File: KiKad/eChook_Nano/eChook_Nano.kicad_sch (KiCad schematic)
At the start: 86 parts, among them J1 Expansion, Q2 Q_NMOS-D_Generic_GSD, Q3 Q_NMOS-D_Generic_GSD, U1 Arduino_Nano_v3.x, U2 TSR_1-2450, U3 MCP6002-xP

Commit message: Updated to BAT54S diodes. Added protection on all inputs
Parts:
- removed D1, D2, D4, D5, D6: SBD, Diode_SMD:D_SOD-523, symbol Device:D_Schottky
- added D1, D13, D14, D15, D16, D17, D18, D19, D2, D20, D4, D5, D6: BAT54S, Package_TO_SOT_SMD:SOT-23, symbol Diode:BAT54S
- JP1, JP2: now not fitted
- JP3: value SolderJumper_2_Open -> ~; footprint Jumper:SolderJumper-2_P1.3mm_Open_RoundedPad1.0x1.5mm -> Jumper:SolderJumper-2_P1.3mm_Bridged_RoundedPad1.0x1.5mm; symbol Jumper:SolderJumper_2_Open -> Jumper:SolderJumper_2_Bridged; now not fitted; now in the parts list
- R34: value 10k -> 100k; LCSC C17414 -> (none)
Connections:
- net +5V: now also D1.2 (K), D13.2 (K), D14.2 (K), D15.2 (K), D16.2 (K), D17.2 (K), D18.2 (K), D19.2 (K), D2.2 (K), D20.2 (K), D4.2 (K), D5.2 (K), D6.2 (K)
- net Batt1v: now also D5.3 (COM)
- net BattTotalV: now also D4.3 (COM)
- net Brake: now also D16.3 (COM)
- net DriverButton: now also D17.3 (COM)
- net DriverButton2: now also D18.3 (COM)
- net GND: now also D1.1 (A), D13.1 (A), D14.1 (A), D15.1 (A), D16.1 (A), D17.1 (A), D18.1 (A), D19.1 (A), D2.1 (A), D20.1 (A), D4.1 (A), D5.1 (A), D6.1 (A)
- net MotorRPM: now also D19.3 (COM)
- net Temp1: now also D2.3 (COM)
- net Temp2: now also D1.3 (COM)
- net Throttle: now also D6.3 (COM)
- net WheelRPM: now also D20.3 (COM)
- net at Q3.3 (D), R14.2, R25.1: now also D15.3 (COM)
- net CurrRefIn: now reaches R21.1, R22.2, U3.2 (-)
- net CurrRefIn: now also D13.3 (COM)
- net CurrSenseIn: now reaches R20.1, R23.2, U3.3 (+)
- net CurrSenseIn: now also D14.3 (COM)
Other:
- note added: "Bluetooth Header"
- note added: "Button Inputs"
- note added: "Expansion Header"
- note added: "PWM Output"
- note removed: "Bluetooth Module"
- note removed: "Driver Input"
- note removed: "Expansion Port"
- note removed: "PWM Buffer"
- moved on the sheet: C4, C5, Conn1, Conn4, Conn5, Conn6, Conn7, Conn8, D10, D11, D3, D8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

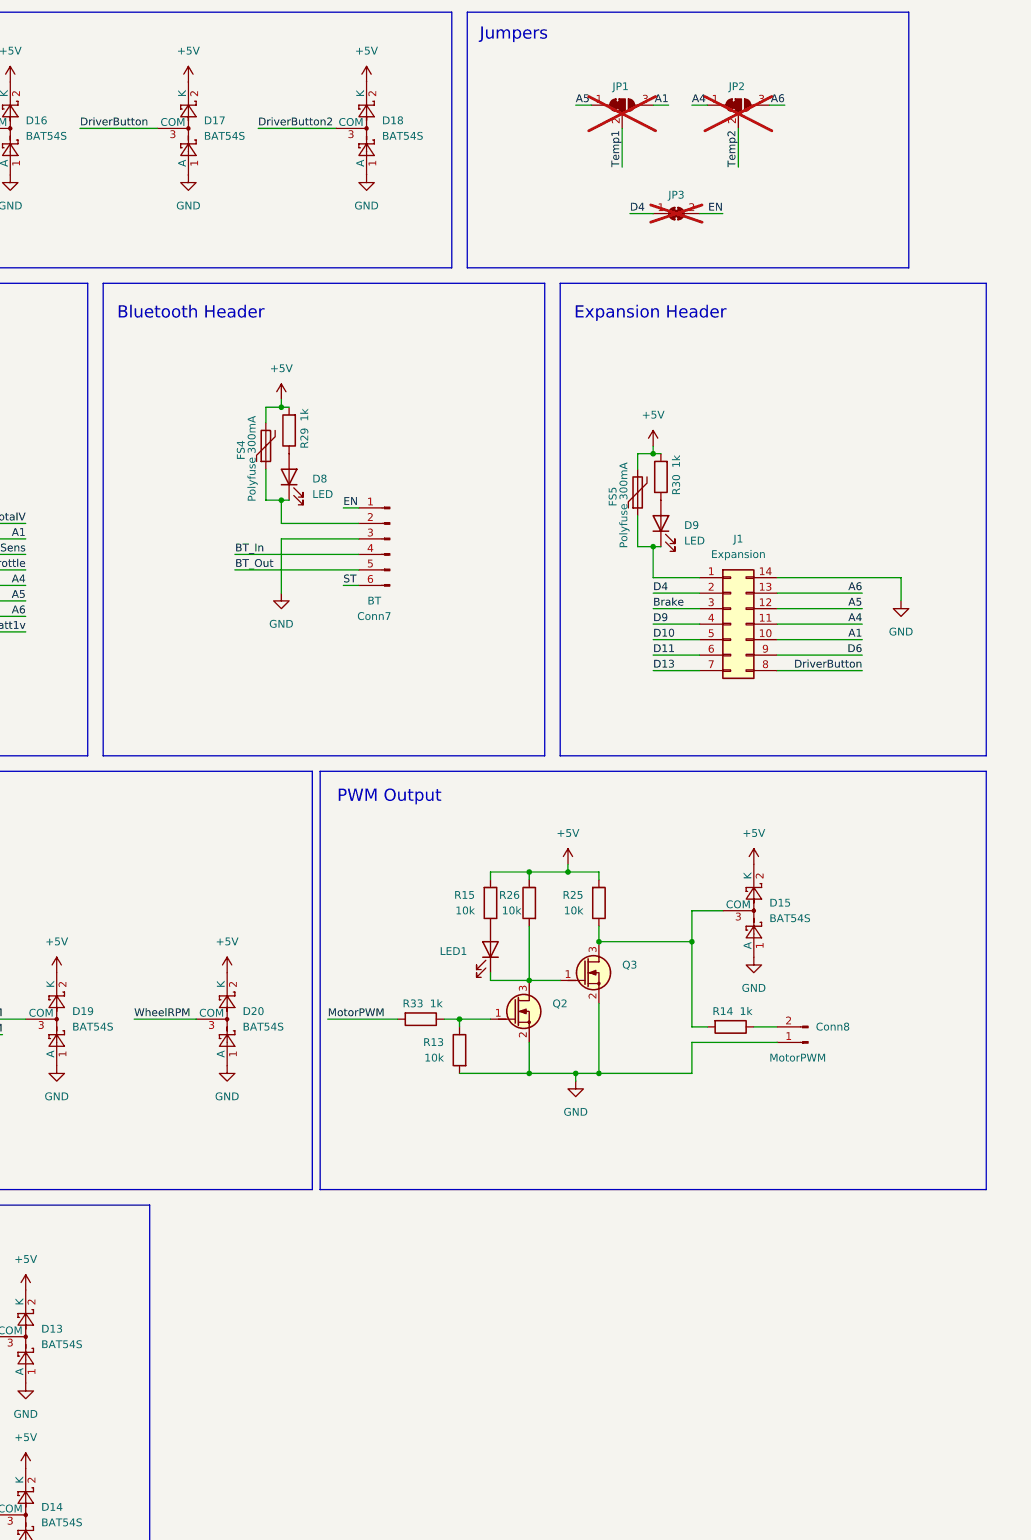
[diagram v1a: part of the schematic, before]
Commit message: Added gate driver PWM output stage
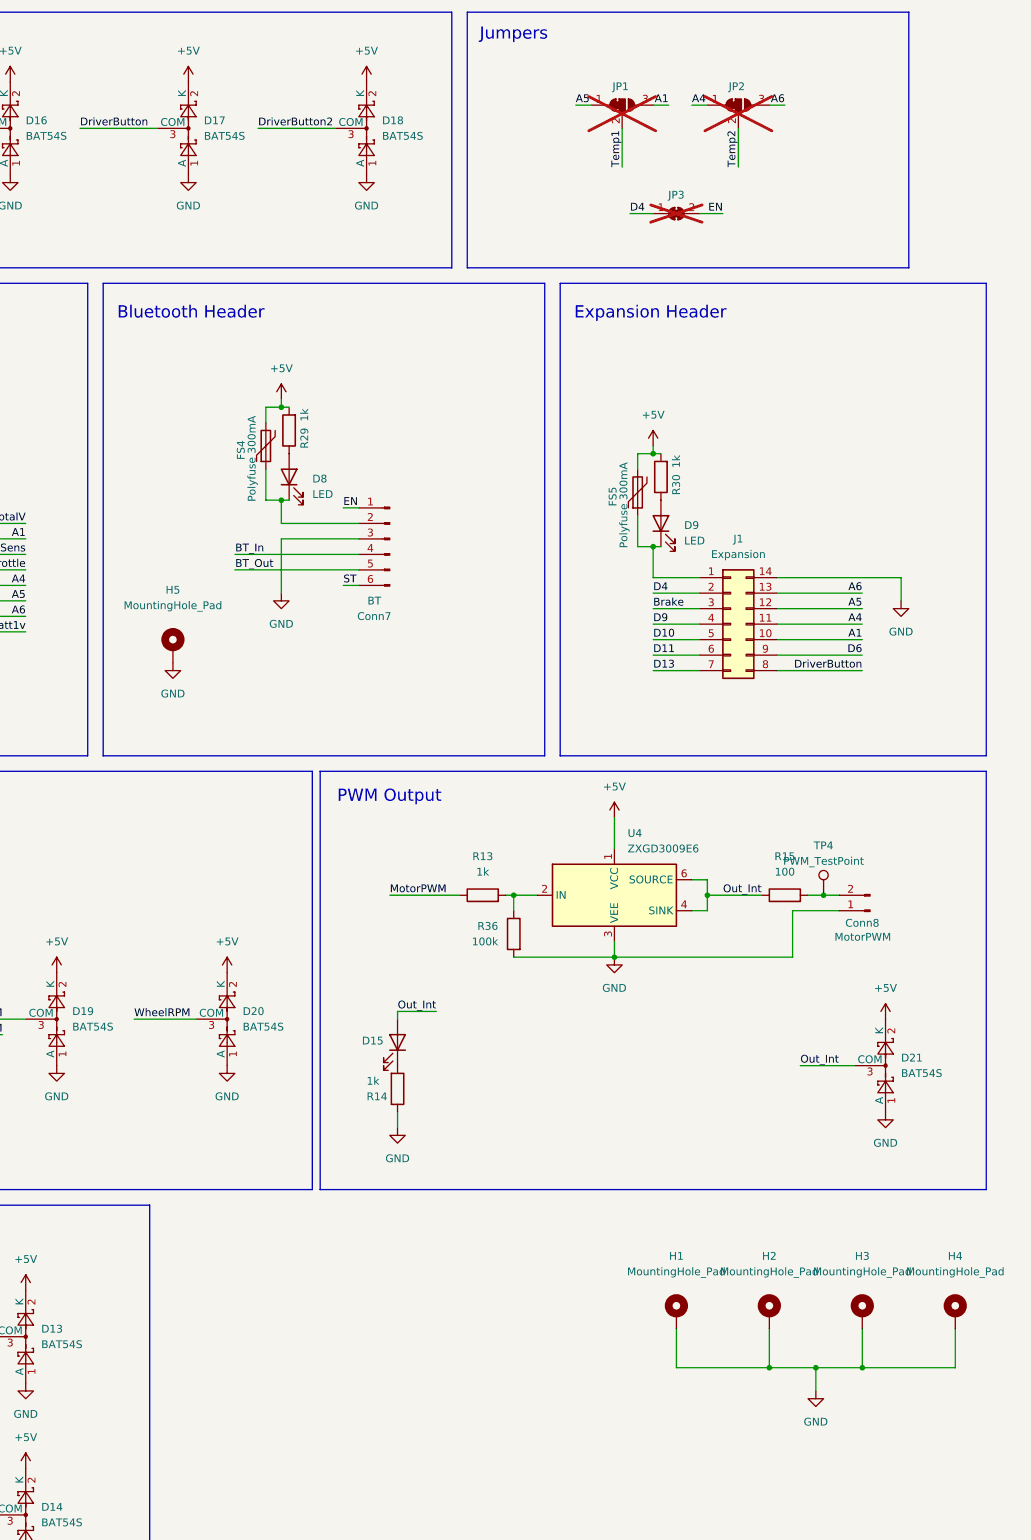
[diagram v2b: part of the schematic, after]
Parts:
- removed D15: BAT54S, Package_TO_SOT_SMD:SOT-23, symbol Diode:BAT54S
- removed LED1: LED_GREEN, LED_SMD:LED_0805_2012Metric, symbol Device:LED
- removed Q2, Q3: Q_NMOS-D_Generic_GSD, PCM_Package_TO_SOT_SMD_AKL:SOT-23, symbol PCM_Transistor_MOSFET_AKL:Q_NMOS-D_Generic_GSD
- removed R25, R26: 10k, Resistor_SMD:R_0805_2012Metric, symbol Device:R
- removed R33: 1k, Resistor_SMD:R_0805_2012Metric, symbol Device:R
- added D15: LED_GREEN, LED_SMD:LED_0805_2012Metric, symbol Device:LED
- added D21: BAT54S, Package_TO_SOT_SMD:SOT-23, symbol Diode:BAT54S
- added H1, H2, H3, H4: MountingHole_Pad, MountingHole:MountingHole_3.2mm_M3_DIN965_Pad_TopBottom, symbol Mechanical:MountingHole_Pad
- added H5: MountingHole_Pad, MountingHole:MountingHole_4.3mm_M4_DIN965_Pad, symbol Mechanical:MountingHole_Pad
- added R36: 100k, Resistor_SMD:R_0805_2012Metric, symbol Device:R
- added TP4: PWM_TestPoint, TestPoint:TestPoint_Pad_D3.0mm, symbol Connector:TestPoint
- added U4: ZXGD3009E6, Package_TO_SOT_SMD:SOT-23-6, symbol Driver_FET:ZXGD3009E6
- R13: value 10k -> 1k; LCSC C17414 -> (none)
- R14: LCSC C17513 -> C17414
- R15: value 10k -> 100; LCSC C17414 -> (none)
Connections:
- net +5V: now also D21.2 (K), U4.1 (VCC); no longer R15.2
- net GND: now also R14.1, D21.1 (A), H1.1, H2.1, H3.1, H4.1, H5.1, R36.2, U4.3 (VEE); no longer R13.2
- net MotorPWM: now also R13.1
- net at R14.2: now also D15.1 (K)
- net at Conn8.2 (Pin_2): now also R15.2, TP4.1; no longer R14.1
- net Out_Int: now reaches R15.1
- net Out_Int: now also D15.2 (A), D21.3 (COM), U4.4 (SINK), U4.6 (SOURCE)
- new net: R13.2, R36.1, U4.2 (IN)
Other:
- moved on the sheet: Conn8

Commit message: Increased PWR LED Resistance, Added mounting holes to SCH
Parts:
- R35: value 10k -> 16k; LCSC C17414 -> C17490
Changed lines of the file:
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@@
 			)
 		)
-		(property "Value" "10k"
+		(property "Value" "16k"
 			(at 147.32 59.69 0)
 			(effects
@@
 			)
 		)
-		(property "LCSC" "C17414"
+		(property "LCSC" "C17490"
 			(at 147.32 62.23 0)
 			(effects

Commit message: As Manufactured V2.1
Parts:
- C2: LCSC C336424 -> C125977
- Conn1, Conn4, Conn5: LCSC C441206 -> C8443
- Conn3, Conn6: LCSC C441205 -> C70914
- FS1, FS2, FS3, FS4, FS5, FS6, FS7: LCSC C18377604 -> C7472522
- J1: LCSC C2685212 -> C38844
- R1, R3: LCSC C17840 -> C21571501
- R13, R15: LCSC (none) -> C17414
- R14: LCSC C17414 -> C17513
- R2, R35, R4: LCSC C17490 -> C706220
- R34, R36: LCSC (none) -> C149504
- U2: LCSC C5369649 -> C19188491
- U4: LCSC (none) -> C156293
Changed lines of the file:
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@@
 			)
 		)
-		(property "LCSC" "C441206"
+		(property "LCSC" "C8443"
 			(at 170.18 173.99 0)
 			(effects
@@
 			)
 		)
+		(property "LCSC" "C17414"
+			(at 299.72 153.67 0)
+			(effects
+				(font
+					(size 1.27 1.27)
+				)
+				(hide yes)
+			)
+		)
 		(pin "2"
 		)
@@
 			)
 		)
-		(property "LCSC" "C441206"
+		(property "LCSC" "C8443"
 			(at 168.91 27.94 0)
 			(effects
@@
 			)
 		)
-		(property "LCSC" "C17490"
+		(property "LCSC" "C706220"
 			(at 85.09 127 0)
 			(effects
@@
 			)
 		)
-		(property "LCSC" "C17490"
+		(property "LCSC" "C706220"
 			(at 147.32 62.23 0)
 			(effects
@@
 			)
 		)
-		(property "LCSC" "C17840"
+		(property "LCSC" "C21571501"
 			(at 34.29 114.3 0)
 			(effects
@@
 			)
 		)
-		(property "LCSC" "C18377604"
+		(property "LCSC" "C7472522"
 			(at 31.75 236.22 90)
 			(effects
@@
 			)
 		)
-		(property "LCSC" "C5369649"
+		(property "LCSC" "C19188491"
 			(at 96.52 49.53 0)
 			(effects
@@
 			)
 		)
-		(property "LCSC" "C17840"
+		(property "LCSC" "C21571501"
 			(at 85.09 114.3 0)
 			(effects
@@
 			)
 		)
-		(property "LCSC" ""
+		(property "LCSC" "C149504"
 			(at 302.26 165.0999 0)
 			(effects
@@
 			)
 		)
-		(property "LCSC" "C18377604"
+		(property "LCSC" "C7472522"
 			(at 264.16 86.36 90)
 			(effects
@@
 			)
 		)
-		(property "LCSC" "C17490"
+		(property "LCSC" "C706220"
 			(at 34.29 127 0)
 			(effects
@@
 			)
 		)
-		(property "LCSC" "C18377604"
+		(property "LCSC" "C7472522"
 			(at 115.57 234.95 90)
 			(effects
@@
 			)
 		)
-		(property "LCSC" "C17414"
+		(property "LCSC" "C17513"
 			(at 280.67 193.04 0)
 			(effects
@@
 			)
 		)
-		(property "LCSC" ""
+		(property "LCSC" "C149504"
 			(at 40.64 256.5399 0)
 			(effects
@@
 			)
 		)
-		(property "LCSC" "C441205"
+		(property "LCSC" "C70914"
 			(at 33.655 185.42 0)
 			(effects
@@
 			)
 		)
-		(property "LCSC" "C441205"
+		(property "LCSC" "C70914"
 			(at 25.4 260.35 0)
 			(effects
@@
 			)
 		)
-		(property "LCSC" "C441206"
+		(property "LCSC" "C8443"
 			(at 106.68 242.57 0)
 			(effects
@@
 			)
 		)
-		(property "LCSC" "C18377604"
+		(property "LCSC" "C7472522"
 			(at 325.12 93.98 90)
 			(effects
@@
 			)
 		)
-		(property "LCSC" "C18377604"
+		(property "LCSC" "C7472522"
 			(at 177.8 165.1 90)
 			(effects
@@
 			)
 		)
-		(property "LCSC" "C18377604"
+		(property "LCSC" "C7472522"
 			(at 52.07 46.99 90)
 			(effects
@@
 			)
 		)
+		(property "LCSC" "C156293"
+			(at 323.4709 149.86 0)
+			(effects
+				(font
+					(size 1.27 1.27)
+				)
+				(hide yes)
+			)
+		)
 		(pin "1"
 		)
@@
 			)
 		)
-		(property "LCSC" "C18377604"
+		(property "LCSC" "C7472522"
 			(at 40.64 38.1 90)
 			(effects
@@
 			)
 		)
+		(property "LCSC" "C17414"
+			(at 349.25 153.67 0)
+			(effects
+				(font
+					(size 1.27 1.27)
+				)
+				(hide yes)
+			)
+		)
 		(pin "2"
 		)
@@
 			)
 		)
-		(property "LCSC" "C336424"
+		(property "LCSC" "C125977"
 			(at 74.93 52.07 0)
 			(effects
@@
 			)
 		)
-		(property "LCSC" "C2685212"
+		(property "LCSC" "C38844"
 			(at 341.63 101.6 0)
 			(effects

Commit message: 24v LED fixed. Improved Routing and Labels
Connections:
- net +5V: now also R35.1
- net GND: no longer R35.1
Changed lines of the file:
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@@
 	(wire
 		(pts
+			(xy 152.4 72.39) (xy 156.21 72.39)
+		)
+		(stroke
+			(width 0)
+			(type default)
+		)
+	)
+	(wire
+		(pts
 			(xy 34.29 245.11) (xy 34.29 251.46)
 		)
@@
 	(wire
 		(pts
+			(xy 156.21 72.39) (xy 156.21 71.12)
+		)
+		(stroke
+			(width 0)
+			(type default)
+		)
+	)
+	(wire
+		(pts
 			(xy 38.1 52.07) (xy 40.64 52.07)
 		)
@@
 	)
 	(symbol
+		(lib_id "power:+5V")
+		(at 156.21 71.12 0)
+		(unit 1)
+		(exclude_from_sim no)
+		(in_bom yes)
+		(on_board yes)
+		(dnp no)
+		(property "Reference" "#PWR035"
+			(at 156.21 74.93 0)
+			(effects
+				(font
+					(size 1.27 1.27)
+				)
+				(hide yes)
+			)
+		)
+		(property "Value" "+5V"
+			(at 156.21 66.04 0)
+			(effects
+				(font
+					(size 1.27 1.27)
+				)
+			)
+		)
+		(property "Footprint" ""
+			(at 156.21 71.12 0)
+			(effects
+				(font
+					(size 1.27 1.27)
+				)
+				(hide yes)
+			)
+		)
+		(property "Datasheet" ""
+			(at 156.21 71.12 0)
+			(effects
+				(font
+					(size 1.27 1.27)
+				)
+				(hide yes)
+			)
+		)
+		(property "Description" ""
+			(at 156.21 71.12 0)
+			(effects
+				(font
+					(size 1.27 1.27)
+				)
+				(hide yes)
+			)
+		)
+		(pin "1"
+		)
+		(instances
+			(project "eChook_Nano"
+				(path "/9538e4ed-27e6-4c37-b989-9859dc0d49e8"
+					(reference "#PWR035")
+					(unit 1)
+				)
+			)
+		)
+	)
+	(symbol
 		(lib_id "Connector:Conn_01x06_Male")
 		(at 284.48 101.6 0)
@@
 					(unit 1)
 				)
-			)
-		)
-	)
-	(symbol
-		(lib_id "power:GND")
-		(at 152.4 72.39 0)
-		(unit 1)
-		(exclude_from_sim no)
-		(in_bom yes)
-		(on_board yes)
-		(dnp no)
-		(fields_autoplaced yes)
-		(property "Reference" "#PWR035"
-			(at 152.4 78.74 0)
-			(effects
-				(font
-					(size 1.27 1.27)
-				)
-				(hide yes)
-			)
-		)
-		(property "Value" "GND"
-			(at 152.4 77.47 0)
-			(effects
-				(font
-					(size 1.27 1.27)
-				)
-			)
-		)
-		(property "Footprint" ""
-			(at 152.4 72.39 0)
-			(effects
-				(font
-					(size 1.27 1.27)
-				)
-				(hide yes)
-			)
-		)
-		(property "Datasheet" ""
-			(at 152.4 72.39 0)
-			(effects
-				(font
-					(size 1.27 1.27)
-				)
-				(hide yes)
-			)
-		)
-		(property "Description" ""
-			(at 152.4 72.39 0)
-			(effects
-				(font
-					(size 1.27 1.27)
-				)
-				(hide yes)
-			)
-		)
-		(pin "1"
-		)
-		(instances
-			(project "eChook_Nano"
-				(path "/9538e4ed-27e6-4c37-b989-9859dc0d49e8"
-					(reference "#PWR035")
-					(unit 1)
-				)
